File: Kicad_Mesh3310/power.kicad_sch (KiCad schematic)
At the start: 21 parts, among them J4 Conn_01x05_Pin, J9 Battery, SW18 POWER ON/OFF, U14 TPS63031DSK, U3 BQ24074RGT, U9 MAX16054

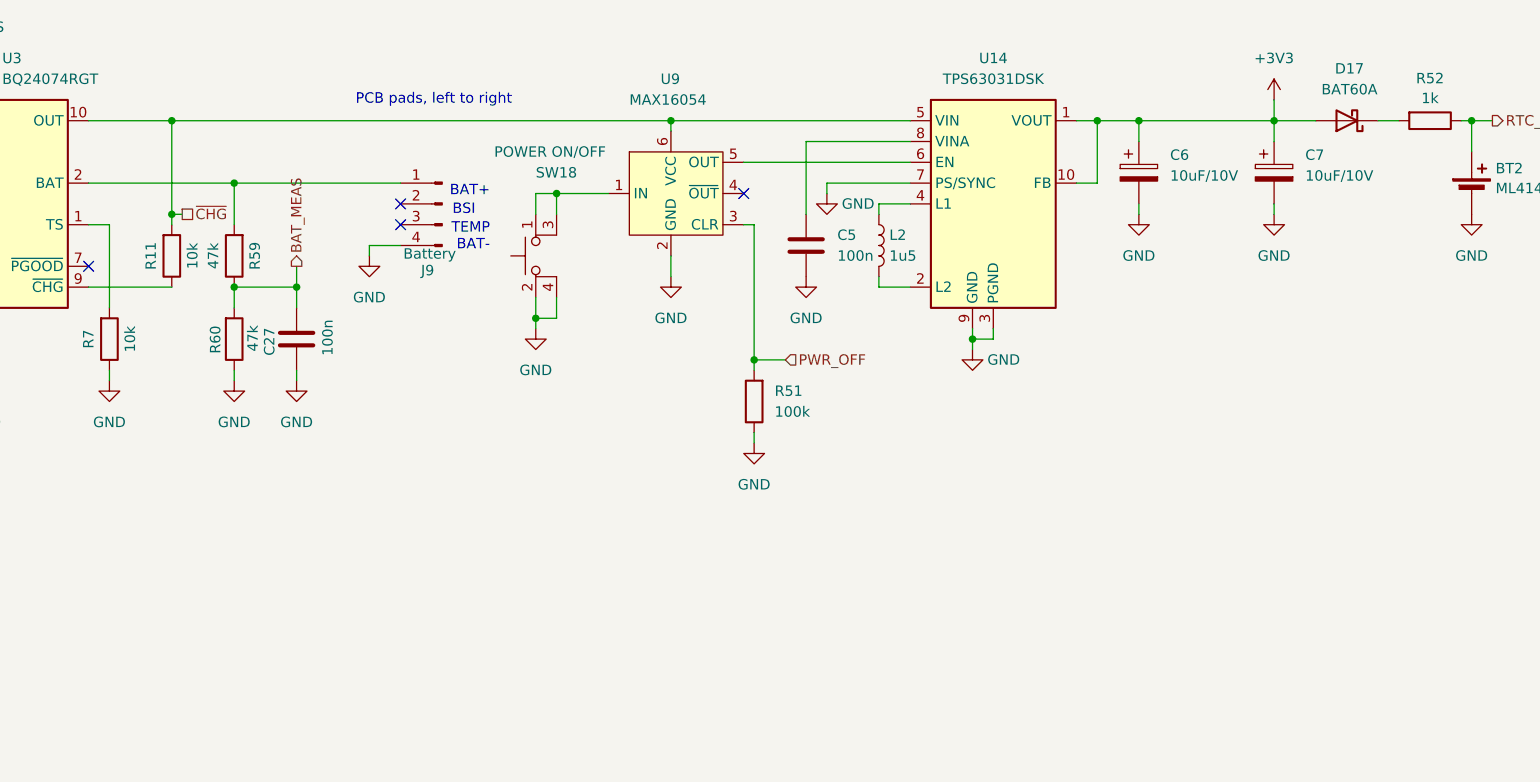
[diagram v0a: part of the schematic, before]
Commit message: Schema afgemaakt, 6-laags layout, LCSC-onderdelen en productiebestanden
- schema opgeschoond en aangevuld (ERC 0)
- bord naar 6 lagen (JLC06161H-3313), volledig gerouteerd, DRC 0
- LTE via U.FL, USB via bodemconnector J4
- LCSC-nummers voor alle onderdelen, datasheets toegevoegd
- gerbers, boorbestanden, positiebestand en stuklijst in productie/
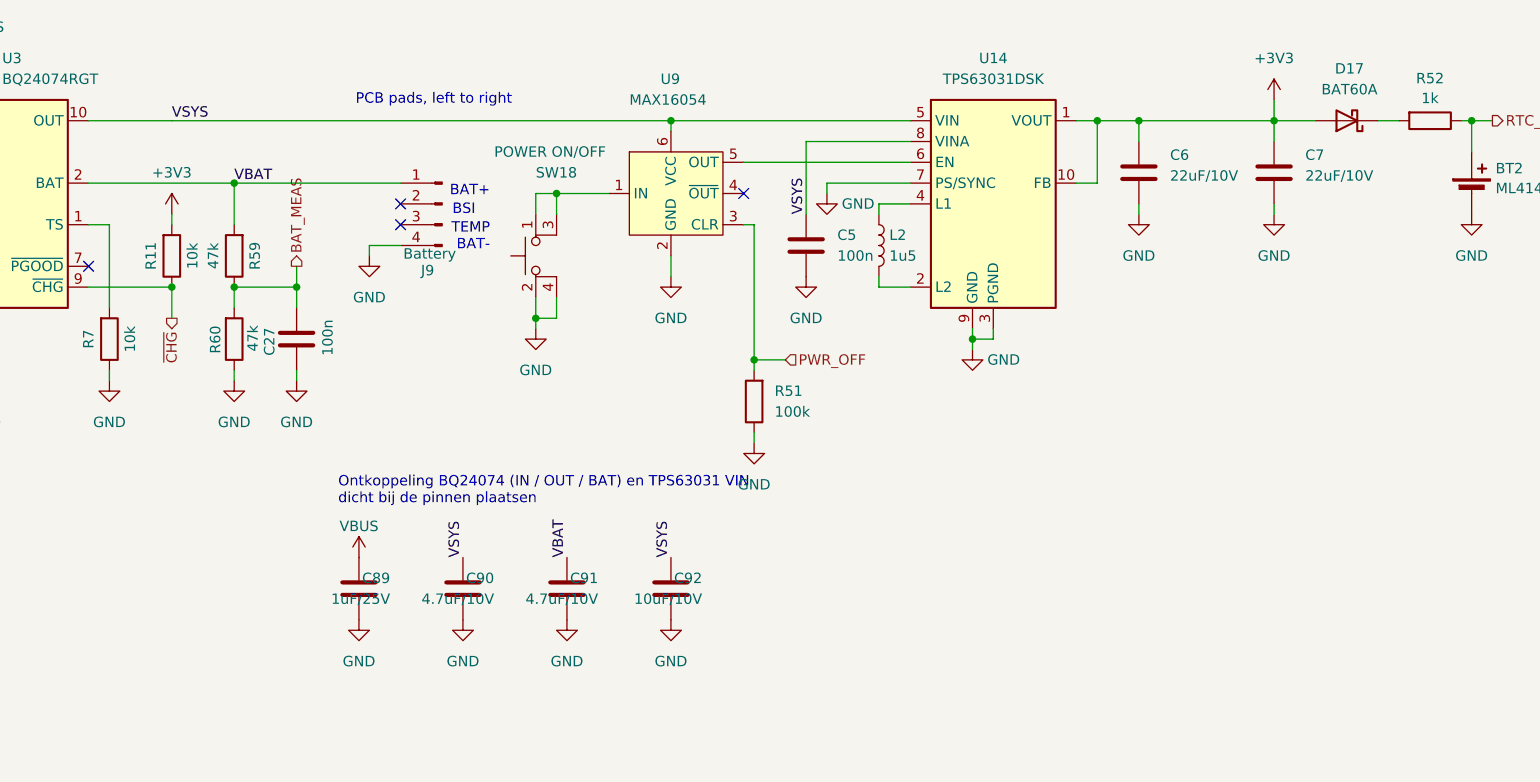
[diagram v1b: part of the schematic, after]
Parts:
- added C89: 1uF/25V, Capacitor_SMD:C_0603_1608Metric, symbol Device:C
- added C90, C91: 4.7uF/10V, Capacitor_SMD:C_0603_1608Metric, symbol Device:C
- added C92: 10uF/10V, Capacitor_SMD:C_0603_1608Metric, symbol Device:C
- C27, C5: LCSC (none) -> C408130
- C6, C7: value 10uF/10V -> 22uF/10V; footprint Capacitor_Tantalum_SMD:CP_EIA-1608-08_AVX-J -> Capacitor_SMD:C_0805_2012Metric; symbol Device:C_Polarized -> Device:C; LCSC (none) -> C45783
- D17: LCSC (none) -> C5355496
- L2: LCSC (none) -> C113080
- R11, R7: LCSC (none) -> C3152038
- R4, R52: LCSC (none) -> C3152043
- R5: LCSC (none) -> C473538
- R51: LCSC (none) -> C3152012
- R59, R60: LCSC (none) -> C304544
- SW18: LCSC (none) -> C128539
- U14: LCSC (none) -> C15516
- U3: LCSC (none) -> C54313
- U9: LCSC (none) -> C79401
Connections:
- net +3V3: now also R11.2
- net GND: now also C89.2, C90.2, C91.2, C92.2
- net VBUS: now also C89.1
- net ~{CHG}: now also R11.1, U3.9 (~{CHG}); no longer R11.2, U14.5 (VIN), U3.10 (OUT), U3.11 (OUT), U9.6 (VCC)
- net VSYS: now reaches C5.2, U14.8 (VINA)
- net VSYS: now also U14.5 (VIN), U3.10 (OUT), U3.11 (OUT), U9.6 (VCC), C90.1, C92.1
- net VBAT: now reaches J9.1 (Pin_1), R59.2, U3.2 (BAT), U3.3 (BAT)
- net VBAT: now also C91.1
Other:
- note added: "Ontkoppeling BQ24074 (IN / OUT / BAT) en TPS63031 VIN dicht bij de pinnen plaatsen"

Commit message: Rev. C: schemafixes uit datasheetcontrole (VDD-buffer nRF9151, DC-blok LoRa, DNP C70/C71/BT2, deler 1M, laadtimers aan)
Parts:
- BT2: now not fitted
- D17, R52: now not fitted; now left out of the parts list
- R59, R60: value 47k -> 1M; LCSC C304544 -> C473482
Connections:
- net GND: no longer U3.14 (TMR)
- no-connect marks 5 -> 6
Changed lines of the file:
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@@
 	)
 	(no_connect
+		(at 62.23 87.63)
+	)
+	(no_connect
 		(at 167.64 88.9)
 	)
@@
 	(wire
 		(pts
-			(xy 43.18 87.63) (xy 62.23 87.63)
-		)
-		(stroke
-			(width 0)
-			(type default)
-		)
-	)
-	(wire
-		(pts
 			(xy 62.23 100.33) (xy 62.23 102.87)
 		)
@@
 	(wire
 		(pts
-			(xy 43.18 87.63) (xy 43.18 111.76)
-		)
-		(stroke
-			(width 0)
-			(type default)
-		)
-	)
-	(wire
-		(pts
 			(xy 175.26 82.55) (xy 175.26 91.44)
 		)
@@
 			)
 		)
-		(property "Value" "47k"
+		(property "Value" "1M"
 			(at 107.696 108.204 90)
 			(effects
@@
 			)
 		)
-		(property "LCSC" "C304544"
+		(property "LCSC" "C473482"
 			(at 103.632 106.68 90)
 			(effects
@@
 		(in_bom no)
 		(on_board yes)
-		(dnp no)
+		(dnp yes)
 		(fields_autoplaced yes)
 		(property "Reference" "BT2"
@@
 	(symbol
 		(lib_id "power:GND")
-		(at 43.18 111.76 0)
-		(unit 1)
-		(exclude_from_sim no)
-		(in_bom yes)
-		(on_board yes)
-		(dnp no)
-		(fields_autoplaced yes)
-		(property "Reference" "#PWR077"
-			(at 43.18 118.11 0)
-			(effects
-				(font
-					(size 1.27 1.27)
-				)
-				(hide yes)
-			)
-		)
-		(property "Value" "GND"
-			(at 43.18 116.84 0)
-			(effects
-				(font
-					(size 1.27 1.27)
-				)
-			)
-		)
-		(property "Footprint" ""
-			(at 43.18 111.76 0)
-			(effects
-				(font
-					(size 1.27 1.27)
-				)
-				(hide yes)
-			)
-		)
-		(property "Datasheet" ""
-			(at 43.18 111.76 0)
-			(effects
-				(font
-					(size 1.27 1.27)
-				)
-				(hide yes)
-			)
-		)
-		(property "Description" "Power symbol creates a global label with name \"GND\" , ground"
-			(at 43.18 111.76 0)
-			(effects
-				(font
-					(size 1.27 1.27)
-				)
-				(hide yes)
-			)
-		)
-		(pin "1"
-		)
-		(instances
-			(project "Mesh3310"
-				(path "/8d65c5ef-7a02-4454-aee5-ab9c49e4aeab/cbcf5f36-d6bc-4a44-8f70-36ed899140c5"
-					(reference "#PWR077")
-					(unit 1)
-				)
-			)
-		)
-	)
-	(symbol
-		(lib_id "power:GND")
 		(at 121.92 96.52 0)
 		(mirror y)
@@
 			)
 		)
-		(property "Value" "47k"
+		(property "Value" "1M"
 			(at 102.87 96.52 90)
 			(effects
@@
 			)
 		)
-		(property "LCSC" "C304544"
+		(property "LCSC" "C473482"
 			(at 107.188 96.52 90)
 			(effects
@@
 		(unit 1)
 		(exclude_from_sim no)
-		(in_bom yes)
+		(in_bom no)
 		(on_board yes)
-		(dnp no)
+		(dnp yes)
 		(fields_autoplaced yes)
 		(property "Reference" "D17"
@@
 		(unit 1)
 		(exclude_from_sim no)
-		(in_bom yes)
+		(in_bom no)
 		(on_board yes)
-		(dnp no)
+		(dnp yes)
 		(fields_autoplaced yes)
 		(property "Reference" "R52"

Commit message: Rev. D/E: nRF9151 op VSYS, aan/uit-knop kort=firmware lang=uit, 3V3 na ENABLE, buffer VSYS
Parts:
- added C100: 100n, Capacitor_SMD:C_0201_0603Metric, symbol Device:C
- added C97, C98, C99: 47uF/6.3V, Capacitor_SMD:C_0805_2012Metric, symbol Device:C
- added D18: 1N4148WS, Diode_SMD:D_SOD-323, symbol Diode:BAT60A
- added D19, D20: BAT60A, Diode_SMD:D_SOD-323, symbol Diode:BAT60A
- added Q8, Q9: BSS138, Package_TO_SOT_SMD:SOT-23, symbol Transistor_FET:BSS138
- added R62, R64: 1M, Resistor_SMD:R_0201_0603Metric, symbol Device:R
- added R63: 47k, Resistor_SMD:R_0201_0603Metric, symbol Device:R
- R51: value 100k -> 330k; LCSC C3152012 -> C270349
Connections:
- net +3V3: now also R62.1, R63.1
- net GND: now also C100.2, C97.2, C98.2, C99.2, Q9.2 (S)
- net PWR_OFF: now also D19.1 (K)
- net RTC_BATT: now also D18.2 (A)
- net VBUS: no longer U3.6 (EN1)
- net VSYS: now also U3.6 (EN1), C99.1
- net EN_3V3: now reaches U14.6 (EN)
- net EN_3V3: now also C100.1, D20.2 (A), R64.2; no longer U9.5 (OUT)
- net KNOP: now reaches SW18.1, SW18.3 (K)
- net KNOP: now also D18.1 (K), Q8.2 (S), Q9.1 (G), R62.2; no longer U9.1 (IN)
- net PWR_ENn: now reaches U9.4 (~{OUT})
- net PWR_ENn: now also Q8.1 (G)
- new net KNOP_IN: Q8.3 (D), U9.1 (IN)
- new net LANG_T: C97.1, C98.1, D19.2 (A), Q9.3 (D), R63.2
- new net PWR_EN: D20.1 (K), R64.1, U9.5 (OUT)
- no-connect marks 6 -> 5
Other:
- note added: "SW18 aan/uit: korte druk als uit = aan (MAX16054). Aan: Q8 blokkeert de knop; firmware leest hem op P0.26 (laag = ingedrukt, pull-up aan) en doet zelf standby / uit via P0.02 (hoog). Lang ingedrukt (~3 s): C97/C98 laden via R63, D19 trekt CLR hoog = voeding hard uit, ook als de firmware hangt. P0.02 nooit laag sturen (ingang laten, alleen hoog om uit te zetten)."
- note added: "U14 (3V3) start via R64/C100 pas 12-51 ms na PWR_EN: Nordic wil VDD_GPIO van de nRF9151 >6 ms na ENABLE. D20 zet 3V3 meteen uit bij uitschakelen."
